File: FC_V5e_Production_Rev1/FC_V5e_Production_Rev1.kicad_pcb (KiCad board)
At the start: 4 copper layers, 88 x 94.5 mm, 260 parts, among them IC3 RV-3028-C7_32.768kHz_1ppm_TA_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, IC6 LT3652IMSE#PBF, J10 INHIBIT_P2, J11 DF11CZ-12DP-2V(27), J12 USB_C_Receptacle_USB2.0_16P, J14 Battery Input, J16 DEBUG, J17 Face4 (Z- Face), J18 Payload, J19 ISS_INHIBIT, J2 DF11CZ-12DP-2V(27), J20 RBF_Inhibit, J21 Heater Output, J22 SWD Port, J23 Aux Deploy 1, J24 Deploy 2, J29 INHIBIT_S2, J3 Life Makes Lemonade, J4 Conn_01x02, J5 BM04B-SRSS-TB(LF)(SN), J7 INHIBIT_P1, J8 INHIBIT_S1, SW1 KMR2, SW2 KMR2, U1 TLV1704, U10 TPS54226PWPRPWP14_2P31X2P46-L, U11 W25Q128JVS, U12 LT8610ABEMSE#TRPBF, U13 E22-400M30S, U14 TCA4307DGKR, U15 LIS2MDL, U16 INA219AxDCN, U18 RP2350_60QFN, U19 AP22653AW6-7, U2 ZDSD04GLGEAG, U21 AP22653AW6-7, U22 AP22653AW6-7, U23 AP22653AW6-7, U24 AP22653AW6-7, U25 TPS2HB50AQPWPRQ1, U27 AP22653AW6-7, U29 AP22653AW6-7, U3 TCA9548APWR, U30 E28-2G4M27S, U5 APS1604M-3SQR-SN_C18214056, U6 TPS4H160AQPWPRQ1, U7 LSM6DSOTR, U8 INA219AxDCN, U9 MCP23017_SS, Y1 ABM8-272-T3

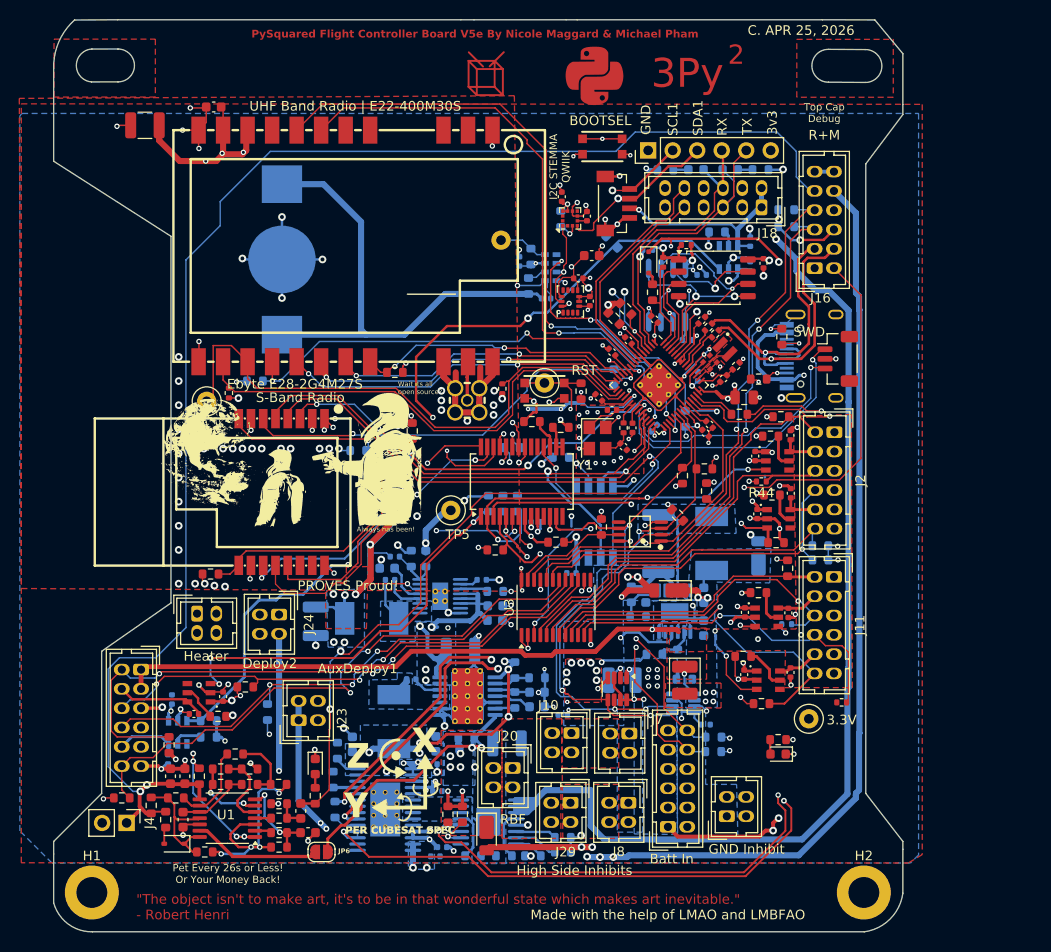
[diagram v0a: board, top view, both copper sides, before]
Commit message: V5e_Rev1: Shifted USB Port Up
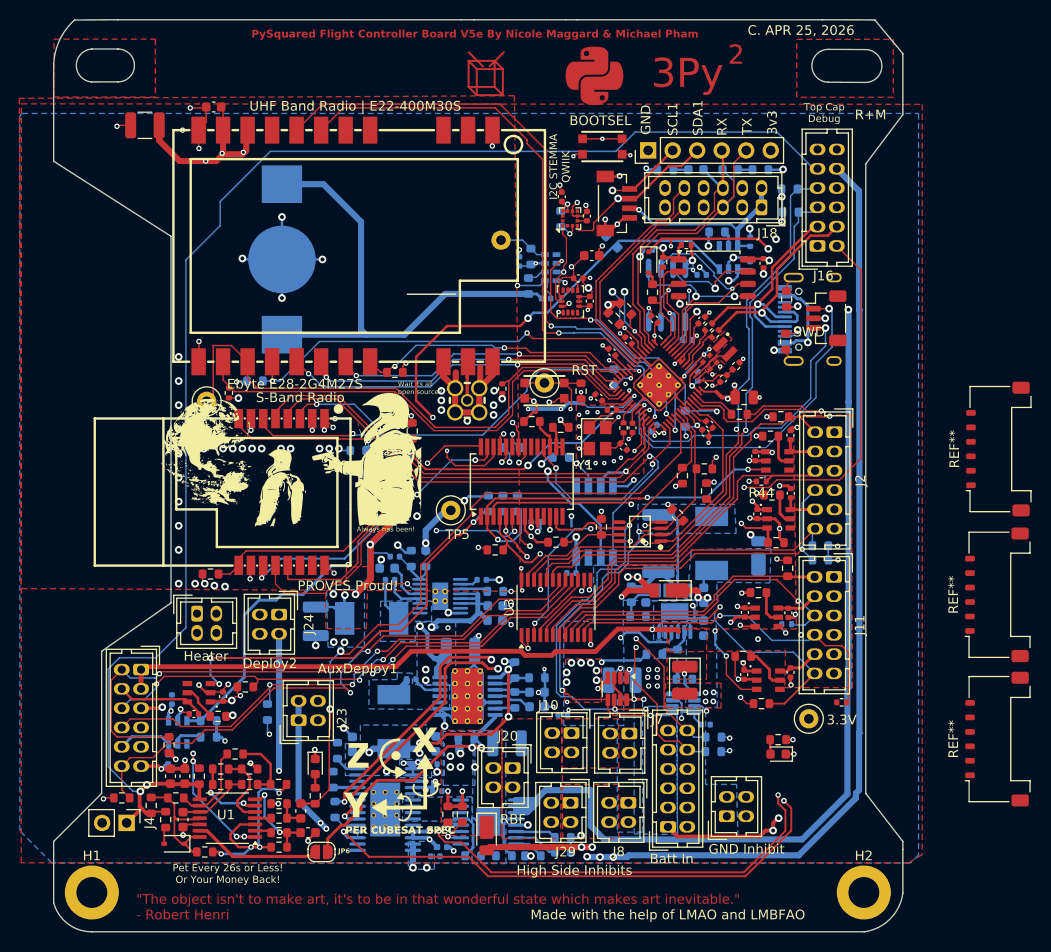
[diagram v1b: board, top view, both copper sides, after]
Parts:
- added REF**: Molex_Pico-Lock_504050-0691_1x06-1MP_P1.50mm_Horizontal, Connector_Molex:Molex_Pico-Lock_504050-0691_1x06-1MP_P1.50mm_Horizontal, F.Cu at (241.1, 107.2)
- added REF**: Molex_Pico-Lock_504050-0691_1x06-1MP_P1.50mm_Horizontal, Connector_Molex:Molex_Pico-Lock_504050-0691_1x06-1MP_P1.50mm_Horizontal, F.Cu at (241.2, 92.0)
- added REF**: Molex_Pico-Lock_504050-0691_1x06-1MP_P1.50mm_Horizontal, Connector_Molex:Molex_Pico-Lock_504050-0691_1x06-1MP_P1.50mm_Horizontal, F.Cu at (241.1, 122.1)
- moved R27 4.80 mm to (219.2, 80.9), turned to 90 degrees
- moved J22 4.37 mm to (223.4, 78.5)
- moved R26 3.93 mm to (219.3, 76.5)
- moved J12 3.82 mm to (223.2, 78.6)
- moved J16 2.32 mm to (222.5, 71.0)
- moved R105 2.18 mm to (219.6, 65.1)
- moved R106 1.57 mm to (219.7, 67.5)
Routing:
- net SWCLK: track 31.0 -> 36.8 mm
- net +3V3: track 218.2 -> 213.1 mm
- net USB_D-: track 29.6 -> 24.7 mm
- net SWDIO: track 28.2 -> 32.6 mm
- net GND: track 256.3 -> 252.0 mm, vias 166 -> 164
- net USB_D+: track 29.4 -> 25.3 mm
- net FC_RESET: track 70.4 -> 72.6 mm
- net DEPLOY1: track 118.4 -> 120.6 mm
- net PAYLOAD_BATT: track 121.0 -> 122.9 mm, vias 1 -> 2
- net Dir_Chrg_In: track 85.8 -> 87.6 mm
- net WDT_DISABLE: track 153.7 -> 151.9 mm
- net Net-(J12-CC2): track 2.36 -> 3.14 mm
- net VBUS: track 97.8 -> 97.1 mm
- net SDA_Top: track 57.4 -> 57.9 mm, vias 2 -> 1
- net SCL_Top: track 59.7 -> 60.1 mm, vias 2 -> 1
